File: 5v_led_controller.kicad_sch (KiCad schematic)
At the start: 8 parts, among them J1 USB_C_Receptacle_USB2.0_14P, U1 BU33SA5WGWZ-E2, U2 ESP32-C3-MINI-1-N4

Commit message: Completed schema
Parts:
- added C3: 1u, symbol Device:C
- added C4, C5: TBD, symbol Device:C
- added J2, J4, J5, J6: Conn_01x03, symbol Connector_Generic:Conn_01x03
- added J3: UART, symbol Connector_Generic:Conn_01x04
- added J7: Jack-DC, Connector_BarrelJack:BarrelJack_SwitchcraftConxall_RAPC10U_Horizontal, symbol Connector:Jack-DC
- added R3, R4: 10K, symbol Device:R
- added R5, R6: TBD, symbol Device:R
- added SW1, SW2: SW_MEC_5E, symbol Switch:SW_MEC_5E
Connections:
- net +3V3: now also J3.4 (Pin_4), R3.1, R4.1
- net +5V: now also J2.1 (Pin_1), J4.1 (Pin_1), J5.1 (Pin_1), J6.1 (Pin_1), J7.2
- net GND: now also U2.1 (GND), C3.2, C4.2, C5.2, J2.3 (Pin_3), J3.3 (Pin_3), J4.3 (Pin_3), J5.3 (Pin_3), J6.3 (Pin_3), J7.1, SW1.3 (K), SW1.4 (A)
- net at J1.A6 (D+), J1.B6 (D+): now also C5.1, R6.2; no longer U2.27 (IO19)
- net at J1.A7 (D-), J1.B7 (D-): now also C4.1, R5.2; no longer U2.26 (IO18)
- net GPIO1: now reaches U2.13 (IO1)
- net GPIO1: now also J2.2 (Pin_2)
- net GPIO4: now reaches U2.18 (IO4)
- net GPIO4: now also J6.2 (Pin_2)
- net GPIO2: now reaches U2.22 (IO8)
- net GPIO2: now also U2.5 (IO2), J4.2 (Pin_2), SW2.3 (K), SW2.4 (A)
- net GPIO9: now reaches U2.23 (IO9)
- net GPIO9: now also R4.2, SW2.1, SW2.2
- net at U2.30 (RXD0): now also J3.1 (Pin_1)
- net at U2.31 (TXD0): now also J3.2 (Pin_2)
- net GPIO3: now reaches U2.6 (IO3)
- net GPIO3: now also J5.2 (Pin_2)
- net at U2.8 (EN): now also C3.1, R3.2, SW1.1, SW1.2
- new net: R6.1, U2.27 (IO19)
- new net: R5.1, U2.26 (IO18)
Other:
- note added: "5V -> 3V3 @ 500mA Max"
- note added: "Add-on Power"
- note added: "Joint Download Boot Mode Button GPI02 H GPI08 H GPI09 L"
- note added: "Reset + RC Delay"
- note added: "USB-C PD 10k on CC For 5V/3A"
- moved on the sheet: C1, C2, J1, JP1, R1, R2, U1, U2

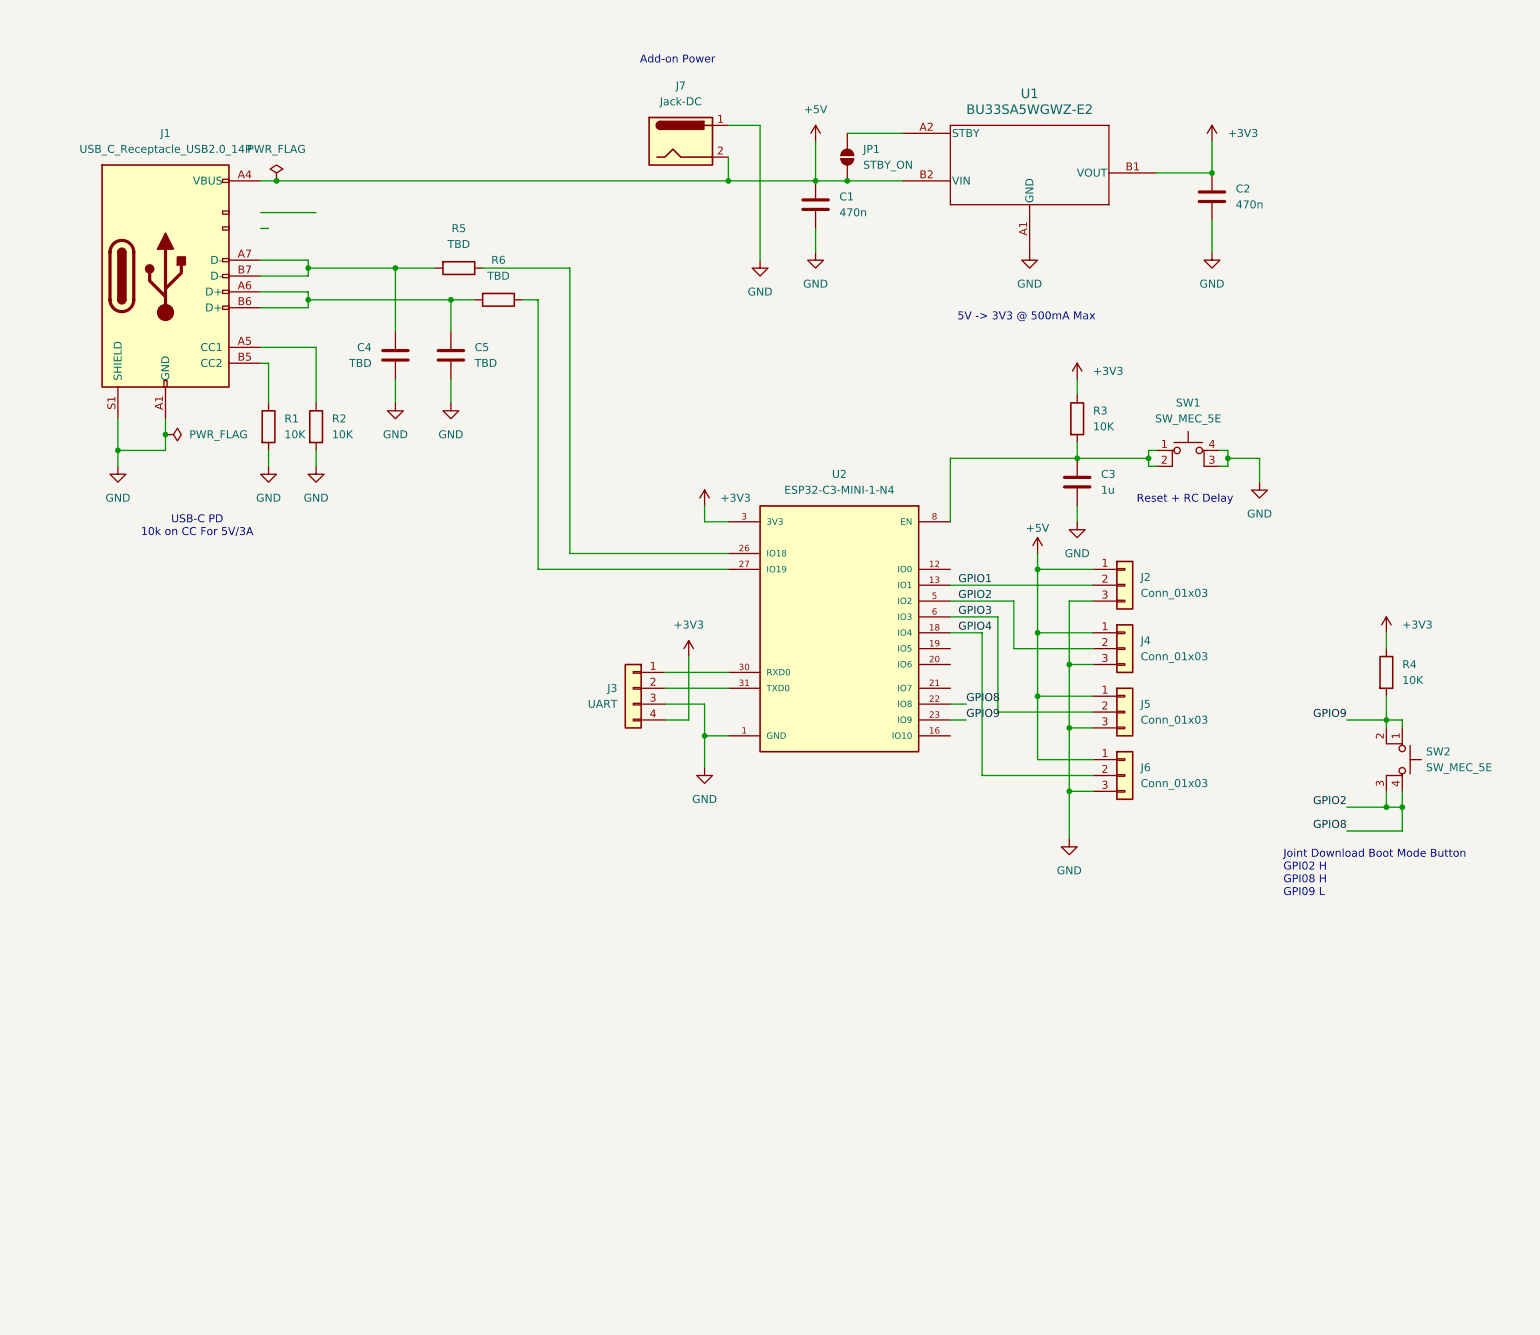
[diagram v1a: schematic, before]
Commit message: Updated Footprints
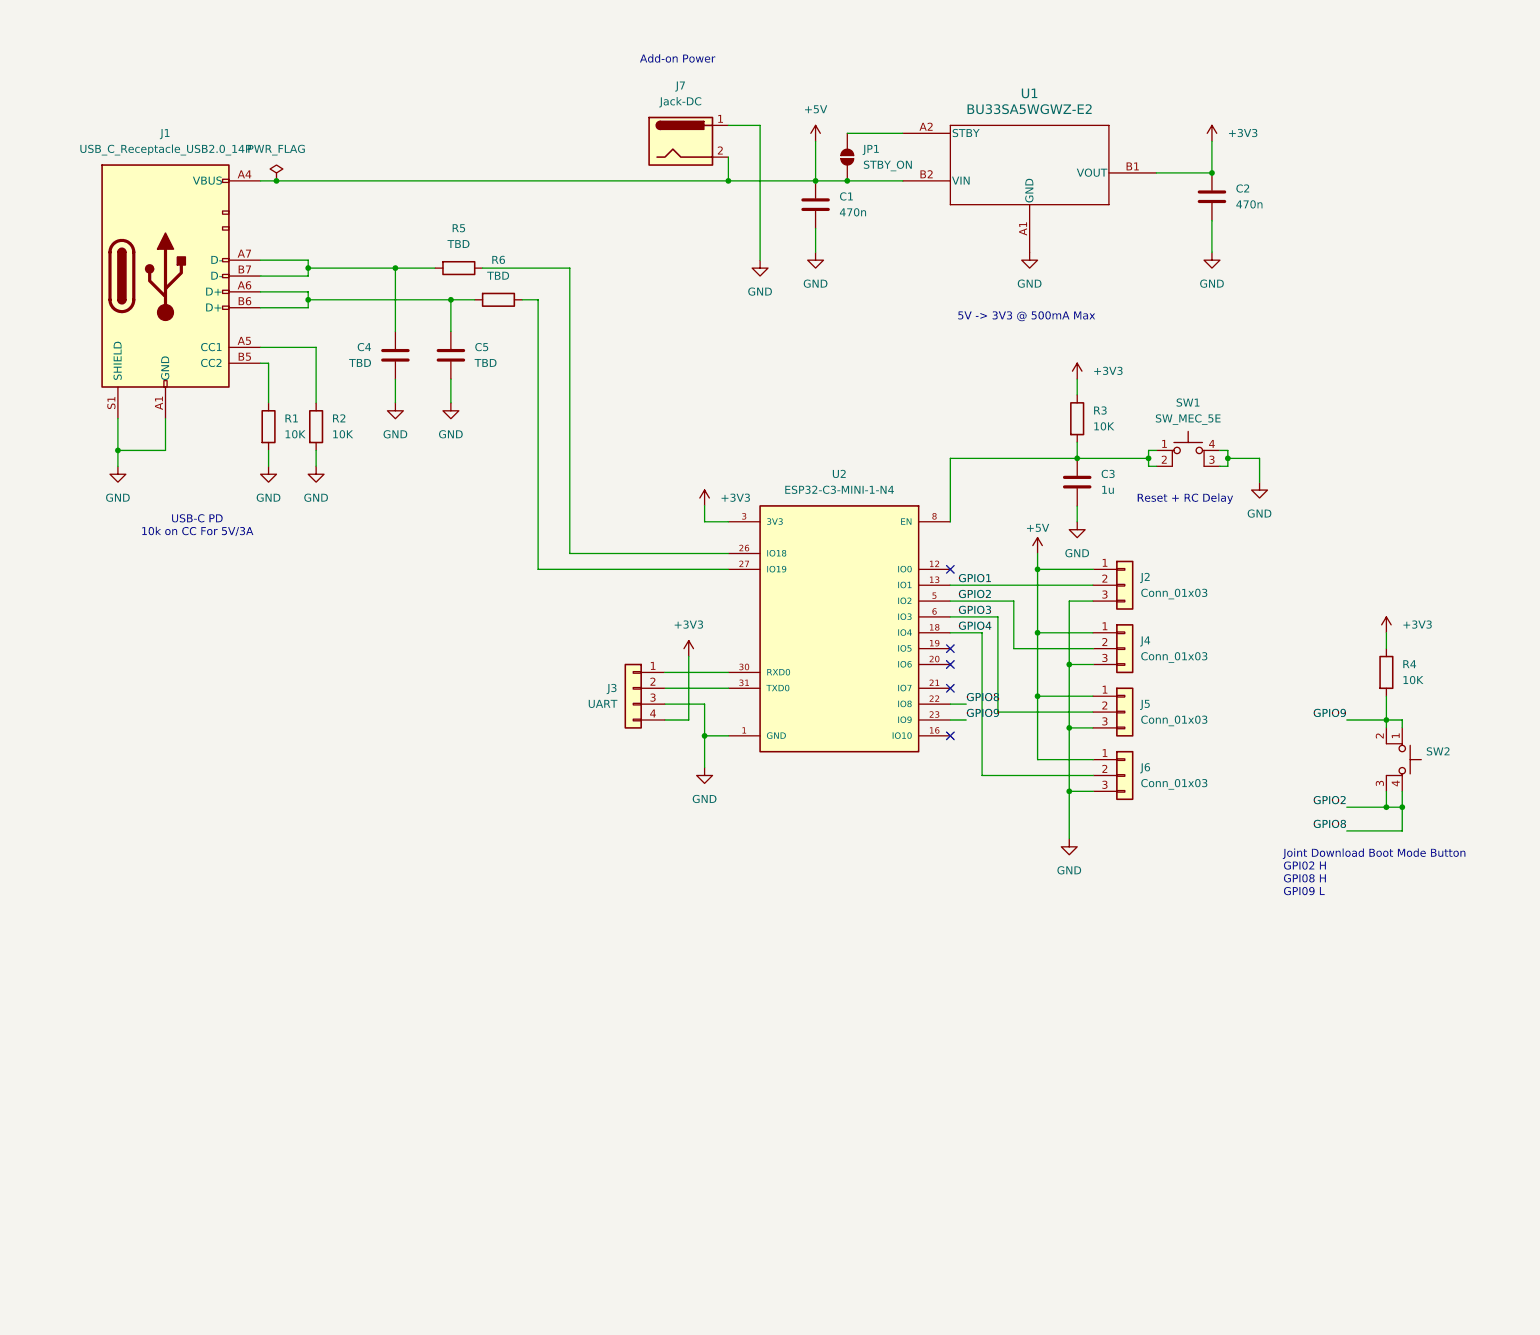
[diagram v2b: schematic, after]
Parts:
- C4: footprint (none) -> Capacitor_SMD:C_0805_2012Metric
- J2: footprint (none) -> Connector_Phoenix_MC_HighVoltage:PhoenixContact_MCV_1,5_3-G-5.08_1x03_P5.08mm_Vertical
- J3: footprint (none) -> Connector_Phoenix_MC:PhoenixContact_MCV_1,5_4-G-3.81_1x04_P3.81mm_Vertical
- JP1: footprint (none) -> Jumper:SolderJumper-2_P1.3mm_Open_RoundedPad1.0x1.5mm
- R2: footprint (none) -> Resistor_SMD:R_1812_4532Metric
- SW2: footprint (none) -> Button_Switch_THT:SW_MEC_5GTH9
- U1: footprint UCSP30L1_ROM -> BU33SA5WGWZ-E2:BU33SA5WGWZ-E2
- U2: footprint ESP32-C3-MINI-1-N4:XCVR_ESP32-C3-MINI-1-N4 -> ESP32-C3-MINI1:ESP32-C3-MINI-1-N4
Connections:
- no-connect marks 0 -> 5
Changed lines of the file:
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@@
 	)
 	(junction
-		(at 44.45 83.82)
-		(diameter 0)
-		(color 0 0 0 0)
-	)
-	(junction
 		(at 153.67 43.18)
 		(diameter 0)
@@
 		(color 0 0 0 0)
 	)
+	(no_connect
+		(at 170.18 105.41)
+	)
+	(no_connect
+		(at 170.18 118.11)
+	)
+	(no_connect
+		(at 170.18 120.65)
+	)
+	(no_connect
+		(at 170.18 124.46)
+	)
+	(no_connect
+		(at 170.18 132.08)
+	)
 	(wire
 		(pts
@@
 	(wire
 		(pts
-			(xy 44.45 83.82) (xy 44.45 86.36)
+			(xy 44.45 81.28) (xy 44.45 86.36)
 		)
 		(stroke
@@
 	(wire
 		(pts
-			(xy 184.15 102.87) (xy 184.15 105.41)
+			(xy 203.2 41.91) (xy 212.09 41.91)
 		)
 		(stroke
@@
 	(wire
 		(pts
-			(xy 59.69 50.8) (xy 60.96 50.8)
+			(xy 184.15 102.87) (xy 184.15 105.41)
 		)
 		(stroke
@@
 	(wire
 		(pts
-			(xy 212.09 41.91) (xy 203.2 41.91)
-		)
-		(stroke
-			(width 0)
-			(type default)
-		)
-	)
-	(wire
-		(pts
 			(xy 214.63 87.63) (xy 214.63 88.9)
 		)
@@
 	(wire
 		(pts
-			(xy 44.45 81.28) (xy 44.45 83.82)
-		)
-		(stroke
-			(width 0)
-			(type default)
-		)
-	)
-	(wire
-		(pts
 			(xy 184.15 135.89) (xy 193.04 135.89)
 		)
@@
 	(wire
 		(pts
-			(xy 59.69 48.26) (xy 68.58 48.26)
-		)
-		(stroke
-			(width 0)
-			(type default)
-		)
-	)
-	(wire
-		(pts
 			(xy 189.23 120.65) (xy 193.04 120.65)
 		)
@@
 			)
 		)
-		(property "Footprint" ""
+		(property "Footprint" "Connector_Phoenix_MC_HighVoltage:PhoenixContact_MCV_1,5_3-G-5.08_1x03_P5.08mm_Vertical"
 			(at 198.12 107.95 0)
 			(effects
@@
 				)
 				(justify left)
+				(hide yes)
 			)
 		)
-		(property "Footprint" ""
+		(property "Footprint" "Button_Switch_THT:SW_MEC_5GTH9"
 			(at 247.65 135.89 0)
 			(effects
@@
 			)
 		)
-		(property "Footprint" ""
+		(property "Footprint" "Jumper:SolderJumper-2_P1.3mm_Open_RoundedPad1.0x1.5mm"
 			(at 153.67 39.37 0)
 			(effects
@@
 	)
 	(symbol
-		(lib_id "power:PWR_FLAG")
-		(at 44.45 83.82 270)
-		(unit 1)
-		(exclude_from_sim no)
-		(in_bom yes)
-		(on_board yes)
-		(dnp no)
-		(fields_autoplaced yes)
-		(property "Reference" "#FLG02"
-			(at 46.355 83.82 0)
-			(effects
-				(font
-					(size 1.27 1.27)
-				)
-				(hide yes)
-			)
-		)
-		(property "Value" "PWR_FLAG"
-			(at 48.26 83.8199 90)
-			(effects
-				(font
-					(size 1.27 1.27)
-				)
-				(justify left)
-			)
-		)
-		(property "Footprint" ""
-			(at 44.45 83.82 0)
-			(effects
-				(font
-					(size 1.27 1.27)
-				)
-				(hide yes)
-			)
-		)
-		(property "Datasheet" "~"
-			(at 44.45 83.82 0)
-			(effects
-				(font
-					(size 1.27 1.27)
-				)
-				(hide yes)
-			)
-		)
-		(property "Description" "Special symbol for telling ERC where power comes from"
-			(at 44.45 83.82 0)
-			(effects
-				(font
-					(size 1.27 1.27)
-				)
-				(hide yes)
-			)
-		)
-		(pin "1"
-		)
-		(instances
-			(project "5v_led_controller"
-				(path "/e68e9797-4f23-4143-bd83-94920fd8fbf0"
-					(reference "#FLG02")
-					(unit 1)
-				)
-			)
-		)
-	)
-	(symbol
 		(lib_id "Connector_Generic:Conn_01x04")
 		(at 119.38 124.46 0)
@@
 			)
 		)
-		(property "Footprint" ""
+		(property "Footprint" "Connector_Phoenix_MC:PhoenixContact_MCV_1,5_4-G-3.81_1x04_P3.81mm_Vertical"
 			(at 119.38 124.46 0)
 			(effects
@@
 			)
 		)
-		(property "Footprint" ""
+		(property "Footprint" "Resistor_SMD:R_1812_4532Metric"
 			(at 66.802 82.55 90)
 			(effects
@@
 			)
 		)
-		(property "Footprint" "UCSP30L1_ROM"
+		(property "Footprint" "BU33SA5WGWZ-E2:BU33SA5WGWZ-E2"
 			(at 162.56 39.37 0)
 			(effects
@@
 			)
 		)
-		(property "Footprint" ""
+		(property "Footprint" "Capacitor_SMD:C_0805_2012Metric"
 			(at 80.3148 74.93 0)
 			(effects
@@
 			)
 		)
-		(property "Footprint" "ESP32-C3-MINI-1-N4:XCVR_ESP32-C3-MINI-1-N4"
+		(property "Footprint" "ESP32-C3-MINI1:ESP32-C3-MINI-1-N4"
 			(at 151.892 87.884 0)
 			(effects
